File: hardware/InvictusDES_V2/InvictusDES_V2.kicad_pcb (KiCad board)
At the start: 4 copper layers, 55.5 x 40.9 mm, 77 parts, among them J1 Screw_Terminal_01x02, J10 USB_B_Micro, J11 Conn_01x06, J12 Micro_SD_Card, J2 Conn_02x05_Odd_Even, J3 Conn_01x06, J9 Conn_01x04, U1 TPSM863257RDXR, U2 STM32F405RGTx, U3 TPS2116DRL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

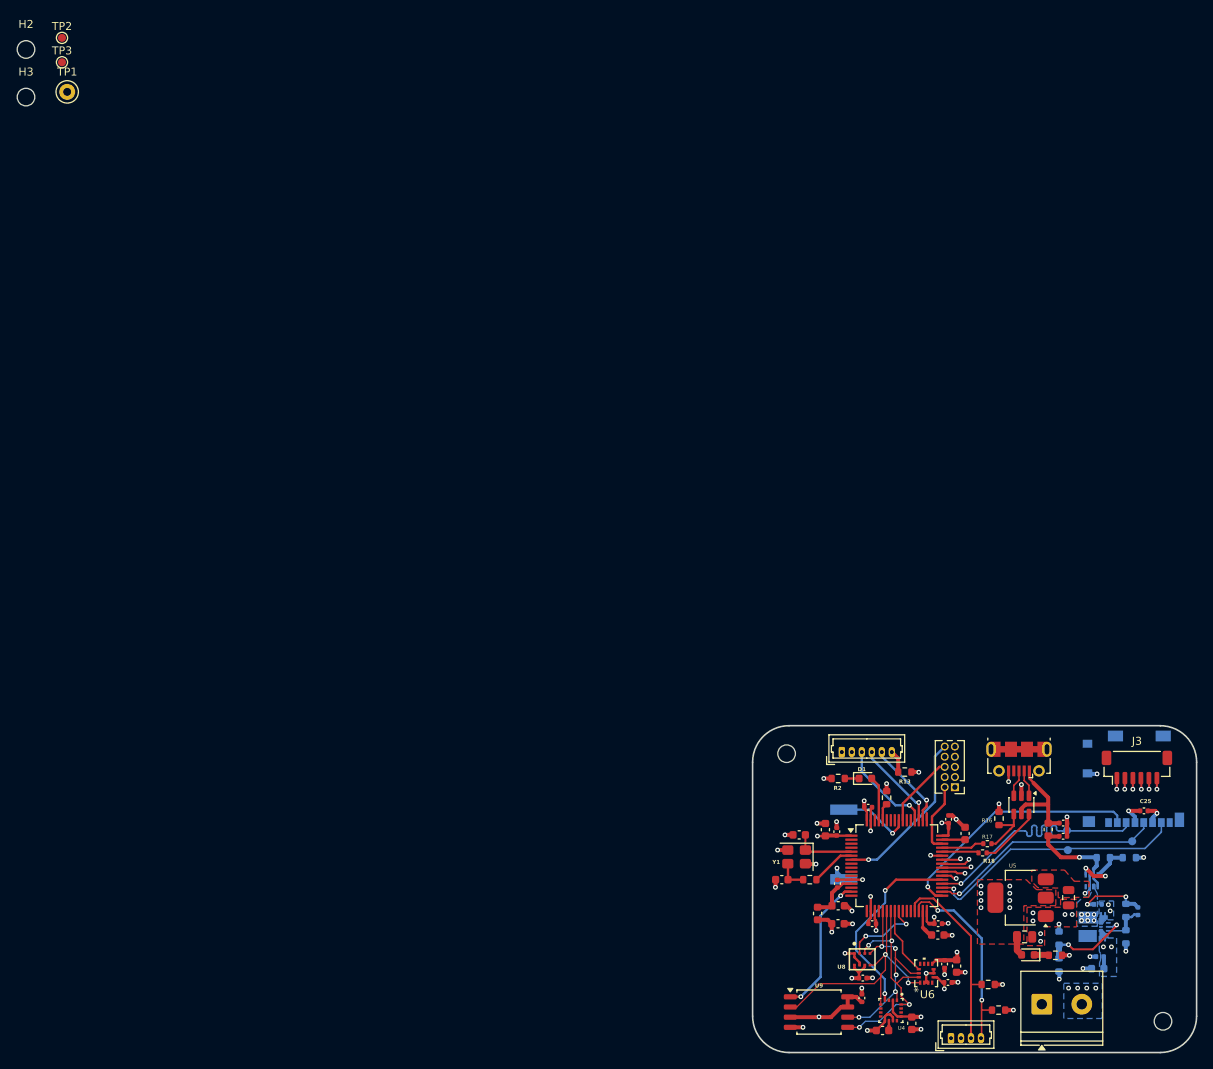
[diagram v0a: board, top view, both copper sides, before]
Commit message: finished PCB, 0 DRC violations, 'logo' made.
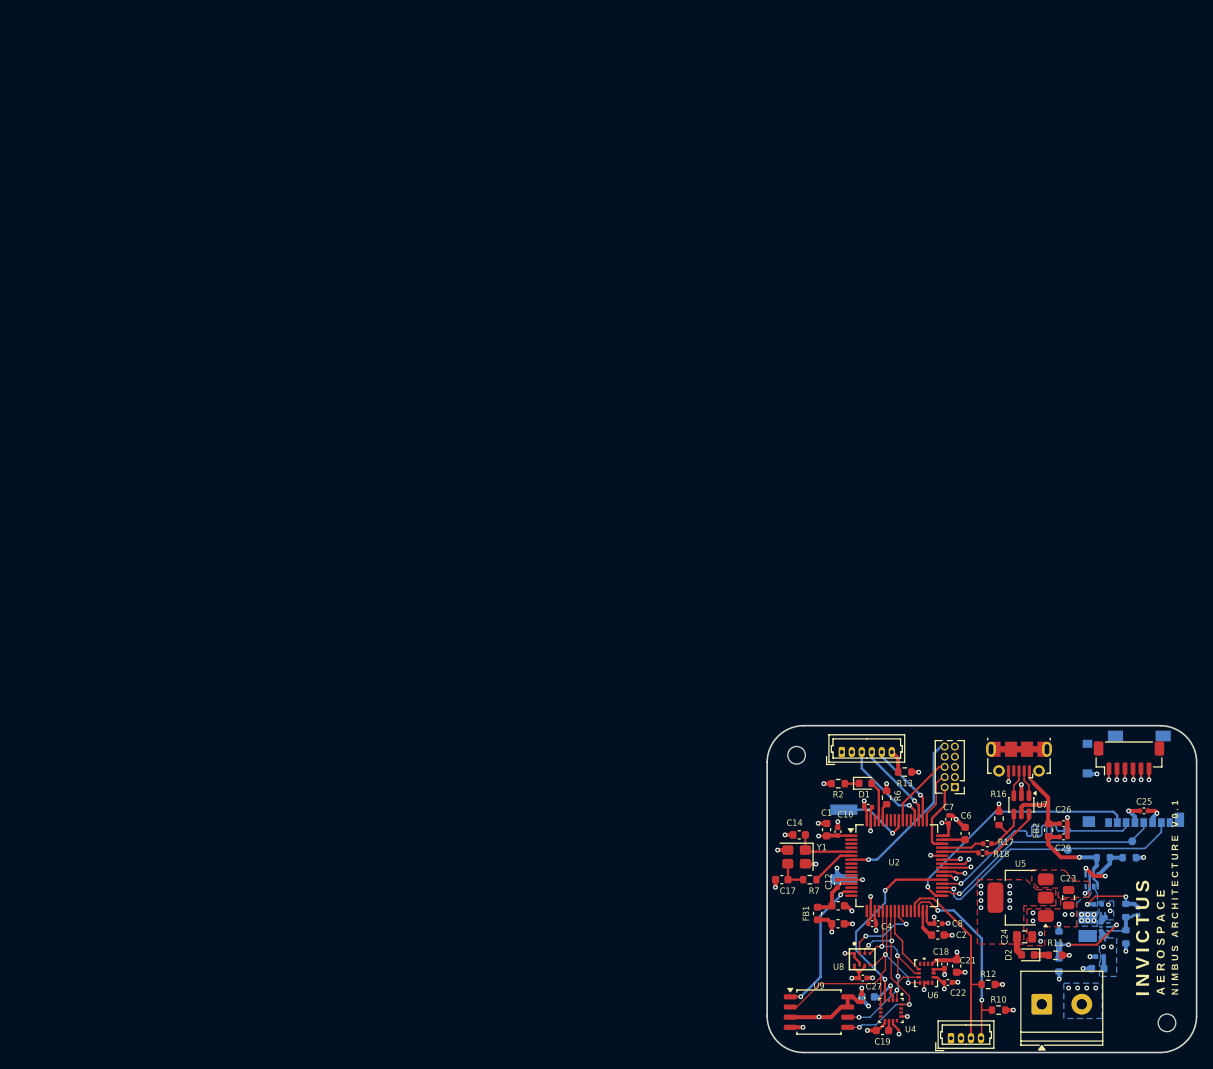
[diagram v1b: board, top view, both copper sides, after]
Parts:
- removed H2, H3: MountingHole_Pad, MountingHole:MountingHole_2.2mm_M2
- removed TP1: TestPoint, TestPoint:TestPoint_Keystone_5000-5004_Miniature
- removed TP2, TP3: TestPoint, TestPoint:TestPoint_Pad_D1.0mm
- added G***: LOGO, LOGO, F.Cu at (144.4, 108.7)
- C20: moved to B.Cu
- moved C20 6.37 mm to (107.8, 120.9), turned to 180 degrees
- moved J3 1.54 mm to (140.3, 91.0)
- moved H1 1.27 mm to (98.8, 90.7)
- moved R2 0.65 mm to (104.0, 94.2)
- moved D1 0.60 mm to (107.4, 94.2)
- moved H4 0.54 mm to (145.1, 124.2)
- moved C1 0.15 mm to (102.5, 100.0)
- moved C10 0.15 mm to (104.0, 100.2)
- moved C26 0.09 mm to (132.2, 99.2)
- moved FB2 0.09 mm to (130.3, 100.0)
- moved C29 0.09 mm to (132.2, 100.9)
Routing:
- net SWCLK: track 0.90 -> 6.50 mm
- net SERVO_6: track 34.2 -> 35.2 mm
- net SERVO_5: track 32.3 -> 33.2 mm
- net SERVO_4: track 30.4 -> 31.1 mm
- net SERVO_3: track 29.2 -> 29.9 mm
- net SERVO_2: track 28.1 -> 28.8 mm
- net SERVO_1: track 29.6 -> 30.2 mm
- net LED_STATUS: track 5.59 -> 4.99 mm
- net USB_D+: track 7.01 -> 6.43 mm
- net Net-(U1-EN): track 11.7 -> 11.1 mm
- net GND: track 69.8 -> 70.2 mm, vias 48 -> 49
- net +3V3: track 56.0 -> 55.7 mm, vias 24 -> 25
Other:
- board size 55.5 x 40.9 mm -> 53.7 x 40.9 mm

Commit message: Adjusted i2c, GPIO breakouts, DRC-passed
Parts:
- moved R10 0.65 mm to (124.0, 121.9)
- moved J9 0.56 mm to (118.1, 125.5)
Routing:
- net I2C2_SDA: track 24.5 -> 23.9 mm
- net I2C2_SCL: track 24.3 -> 23.7 mm
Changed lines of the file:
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@@
 	(footprint "Connector_Molex:Molex_PicoBlade_53047-0410_1x04_P1.25mm_Vertical"
 		(layer "F.Cu")
-		(at 118.1 126.065)
+		(at 118.1 125.505)
 		(descr "Molex PicoBlade Connector System, 53047-0410, 4 Pins per row (http://www.molex.com/pdm_docs/sd/530470610_sd.pdf), generated with kicad-footprint-generator")
 		(tags "connector Molex PicoBlade vertical")
@@
 	(footprint "Resistor_SMD:R_0603_1608Metric"
 		(layer "F.Cu")
-		(at 124.05 122.55 180)
+		(at 124.05 121.9 180)
 		(descr "Resistor SMD 0603 (1608 Metric), square (rectangular) end terminal, IPC-7351 nominal, (Body size source: IPC-SM-782 page 72, https://www.pcb-3d.com/wordpress/wp-content/uploads/ipc-sm-782a_amendment_1_and_2.pdf), generated with kicad-footprint-generator")
 		(tags "resistor")
@@
 		)
 		(fp_text user "${REFERENCE}"
-			(at -0.6975 -1.4 180)
+			(at -0.6975 -1.55 270)
 			(layer "F.SilkS")
 			(effects
@@
 	)
 	(segment
-		(start 125.9 122.55)
-		(end 124.875 122.55)
+		(start 125.9 121.9)
+		(end 124.875 121.9)
 		(width 0.5)
 		(layer "F.Cu")
@@
 	)
 	(via
-		(at 125.9 122.55)
+		(at 125.9 121.9)
 		(size 0.6)
 		(drill 0.3)
@@
 	)
 	(segment
-		(start 121.85 125.865)
-		(end 121.925 125.79)
-		(width 0.25)
-		(layer "F.Cu")
-		(net 32)
-	)
-	(segment
-		(start 121.925 122.55)
-		(end 121.925 121.325)
+		(start 123.225 121.9)
+		(end 121.925 121.9)
 		(width 0.2)
 		(layer "F.Cu")
@@
 	)
 	(segment
-		(start 123.225 122.55)
-		(end 121.925 122.55)
+		(start 121.925 125.43)
+		(end 121.925 121.9)
 		(width 0.2)
 		(layer "F.Cu")
@@
 	)
 	(segment
-		(start 121.85 126.065)
-		(end 121.85 125.865)
-		(width 0.25)
+		(start 115.403 109.053)
+		(end 114.385348 109.053)
+		(width 0.2)
 		(layer "F.Cu")
 		(net 32)
 	)
 	(segment
-		(start 115.403 109.053)
-		(end 114.385348 109.053)
+		(start 121.85 125.505)
+		(end 121.925 125.43)
 		(width 0.2)
 		(layer "F.Cu")
@@
 	)
 	(segment
-		(start 121.925 121.325)
-		(end 121.95 121.3)
-		(width 0.25)
+		(start 121.925 121.9)
+		(end 121.925 120.825)
+		(width 0.2)
 		(layer "F.Cu")
 		(net 32)
 	)
 	(segment
-		(start 121.925 125.79)
-		(end 121.925 122.55)
+		(start 121.925 120.825)
+		(end 121.95 120.8)
 		(width 0.2)
 		(layer "F.Cu")
@@
 	)
 	(via
-		(at 121.95 121.3)
+		(at 121.95 120.8)
 		(size 0.6)
 		(drill 0.3)
@@
 	)
 	(segment
-		(start 118.45 110.1)
-		(end 121.95 113.6)
+		(start 121.95 113.6)
+		(end 118.45 110.1)
 		(width 0.3)
 		(layer "B.Cu")
@@
 	)
 	(segment
-		(start 121.95 113.6)
-		(end 121.95 121.3)
+		(start 118.45 110.1)
+		(end 116.45 110.1)
 		(width 0.3)
 		(layer "B.Cu")
@@
 	)
 	(segment
-		(start 116.45 110.1)
-		(end 118.45 110.1)
+		(start 121.95 120.8)
+		(end 121.95 113.6)
 		(width 0.3)
 		(layer "B.Cu")
@@
 	)
 	(segment
+		(start 120.6 125.505)
+		(end 120.6 119.35)
+		(width 0.254)
+		(layer "F.Cu")
+		(net 33)
+	)
+	(segment
 		(start 113.575 109.22271)
 		(end 114.19771 108.6)
@@
 		(width 0.254)
 		(layer "F.Cu")
-		(net 33)
-	)
-	(segment
-		(start 120.6 126.065)
-		(end 120.6 119.35)
-		(width 0.254)
-		(layer "F.Cu")
